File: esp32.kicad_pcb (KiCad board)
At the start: 2 copper layers, 44 x 100 mm, 129 parts, among them J1 USB_C, J10 UART_2, J11 I2C_0, J12 I2C_1, J13 I2C_2, J14 GND_CONN, J15 SPI_0, J16 SPI_1, J17 SPI_2, J18 PWR_CONN, J2 USB_C_UART, J3 A0, J4 A1, J5 A2, J6 D0, J7 D1, J8 UART_0, J9 UART_1, Q1 S8050, Q10 AO3400A, Q11 AO3400A, Q12 AO3400A, Q2 S8050, Q3 AO3400A, Q4 AO3400A, Q5 AO3400A, Q6 AO3400A, Q7 AO3400A, Q8 AO3400A, Q9 AO3400A, SW1 SW_RST, SW2 SW_BOOT, U1 AMS1117-3.3, U2 XL1509-5.0, U3 ESP32-S3-WROOM-1, U4 CH340C

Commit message: delete unused components
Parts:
- removed C11, C12, C13, C14, C15, C16: 100n, Capacitor_SMD:C_0805_2012Metric_Pad1.18x1.45mm_HandSolder
- removed D4: LED, LED_SMD:LED_0805_2012Metric_Pad1.15x1.40mm_HandSolder
- removed J10: UART_2, Connector_JST:JST_XH_B4B-XH-A_1x04_P2.50mm_Vertical
- removed J11: I2C_0, Connector_JST:JST_XH_B4B-XH-A_1x04_P2.50mm_Vertical
- removed J12: I2C_1, Connector_JST:JST_XH_B4B-XH-A_1x04_P2.50mm_Vertical
- removed J13: I2C_2, Connector_JST:JST_XH_B4B-XH-A_1x04_P2.50mm_Vertical
- removed J18: PWR_CONN, TerminalBlock:TerminalBlock_MaiXu_MX126-5.0-02P_1x02_P5.00mm
- removed J8: UART_0, Connector_JST:JST_XH_B4B-XH-A_1x04_P2.50mm_Vertical
- removed J9: UART_1, Connector_JST:JST_XH_B4B-XH-A_1x04_P2.50mm_Vertical
- removed R7: R, Resistor_SMD:R_0805_2012Metric_Pad1.20x1.40mm_HandSolder
- C17, C6, C8, D1, L1, U2: moved to F.Cu
- J14: value GND_CONN -> PWR_CONN
- moved C8 25.0 mm to (48.2, 35.0), turned to 0 degrees
- moved D5 22.4 mm to (62.0, 33.6), turned to 180 degrees
- moved U2 16.5 mm to (47.1, 42.4), turned to 0 degrees
- moved D1 14.0 mm to (62.4, 24.8), turned to 0 degrees
- moved L1 9.62 mm to (57.9, 40.4), turned to 0 degrees
- moved C17 8.98 mm to (64.8, 40.4), turned to 0 degrees
- moved C6 3.71 mm to (49.6, 25.9)
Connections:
- J14 pad 2: GND -> Net-(D5-A)
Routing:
- net Net-(D4-A): track 1.97 -> 0.00 mm

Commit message: LMR36520 version
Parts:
- removed C17: 47uF, Capacitor_THT:C_Radial_D6.3mm_H5.0mm_P2.50mm
- removed D1: SS34, Diode_SMD:D_SMB-SMC_Universal_Handsoldering
- removed U2: XL1509-5.0, Package_SO:SOIC-8_3.9x4.9mm_P1.27mm
- added C11: 22uF, Capacitor_SMD:C_0805_2012Metric_Pad1.18x1.45mm_HandSolder, F.Cu at (148.1, 83.9)
- added C12: 20pF, Capacitor_SMD:C_0805_2012Metric_Pad1.18x1.45mm_HandSolder, B.Cu at (148.8, 72.5)
- added R53: 43.2k, Resistor_SMD:R_0805_2012Metric_Pad1.20x1.40mm_HandSolder, B.Cu at (143.9, 70.4)
- added R7: 100k, Resistor_SMD:R_0805_2012Metric_Pad1.20x1.40mm_HandSolder, B.Cu at (148.8, 70.4)
- C4: value 10uF -> 4.7uF; moved to B.Cu
- C5: value 100nF -> 220nF; moved to B.Cu
- C6: value 470uF -> 1uF; footprint Capacitor_SMD:CP_Elec_8x10.5 -> Capacitor_SMD:C_0805_2012Metric_Pad1.18x1.45mm_HandSolder
- C7: value 10uF -> 0.1uF
- C8: value 180uF -> 22uF; footprint Capacitor_SMD:CP_Elec_6.3x5.4 -> Capacitor_SMD:C_0805_2012Metric_Pad1.18x1.45mm_HandSolder
- L1: value 68µH -> 10uH; footprint Inductor_SMD:L_6.3x6.3_H3 -> Inductor_SMD:L_Chilisin_BMRA00050530; moved to B.Cu
- U1: value AMS1117-3.3 -> LMR36520ADDAR; footprint Package_TO_SOT_SMD:SOT-223-3_TabPin2 -> Package_SO:Texas_HTSOP-8-1EP_3.9x4.9mm_P1.27mm_EP2.95x4.9mm_Mask2.4x3.1mm_ThermalVias
- moved C8 110.1 mm to (148.0, 81.8), turned to 180 degrees
- moved C6 108.6 mm to (147.0, 73.9), turned to -90 degrees
- moved L1 96.9 mm to (147.2, 78.1)
- moved D5 77.3 mm to (136.2, 55.3)
- moved C7 12.4 mm to (149.4, 73.9), turned to -90 degrees
- moved C4 5.82 mm to (147.0, 66.6), turned to -90 degrees
- moved C5 4.64 mm to (149.1, 66.6), turned to -90 degrees
- moved C20 3.05 mm to (152.2, 79.9)
- moved C18 3.05 mm to (152.3, 92.9)
- moved C19 3.05 mm to (152.3, 86.4)
- moved J15 2.70 mm to (166.4, 92.0)
- moved J16 2.70 mm to (166.4, 85.5)
- moved J17 2.70 mm to (166.4, 79.0)
- moved D3 2.12 mm to (149.3, 57.8)
- moved R6 2.12 mm to (145.3, 57.8)
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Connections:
- C4 pad 1: +3V3 -> VCC
- C5 pad 1: +3V3 -> VCC
- C6 pad 1: VCC -> Net-(U1-VCC)
- C7 pad 1: +5V -> Net-(U1-BOOT)
- C7 pad 2: GND -> Net-(U1-SW)
- C8 pad 1: +5V -> +3V3
- L1 pad 1: Net-(D1-K) -> Net-(U1-SW)
- L1 pad 2: +5V -> +3V3
- U1 pad 2: +3V3 -> VCC
- U1 pad 3: +5V -> VCC
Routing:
- net GND: track 697.3 -> 783.6 mm, vias 4 -> 5
- net +3V3: track 428.9 -> 454.9 mm, vias 26 -> 23
- net VCC: track 0.00 -> 21.6 mm, vias 0 -> 3
- net Net-(U1-SW): track 0.00 -> 10.7 mm, vias 0 -> 1
- net Net-(U1-FB): track 0.00 -> 5.02 mm, vias 0 -> 1
- net /flex_io3/OUT_0: track 4.99 -> 9.36 mm
- net /flex_io3/OUT_1: track 5.48 -> 9.63 mm
- net Net-(D5-A): track 0.00 -> 4.08 mm
- net /A0: track 143.9 -> 139.9 mm
- net Net-(U1-BOOT): track 0.00 -> 2.60 mm
- net Net-(U1-VCC): track 0.00 -> 2.52 mm
- net +5V: track 48.0 -> 45.5 mm, vias 6 -> 5
- net /SPI_CS0: track 55.4 -> 54.3 mm
- net /SPI_SCK: track 49.6 -> 48.5 mm
- net /SPI_MOSI: track 51.0 -> 49.9 mm
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
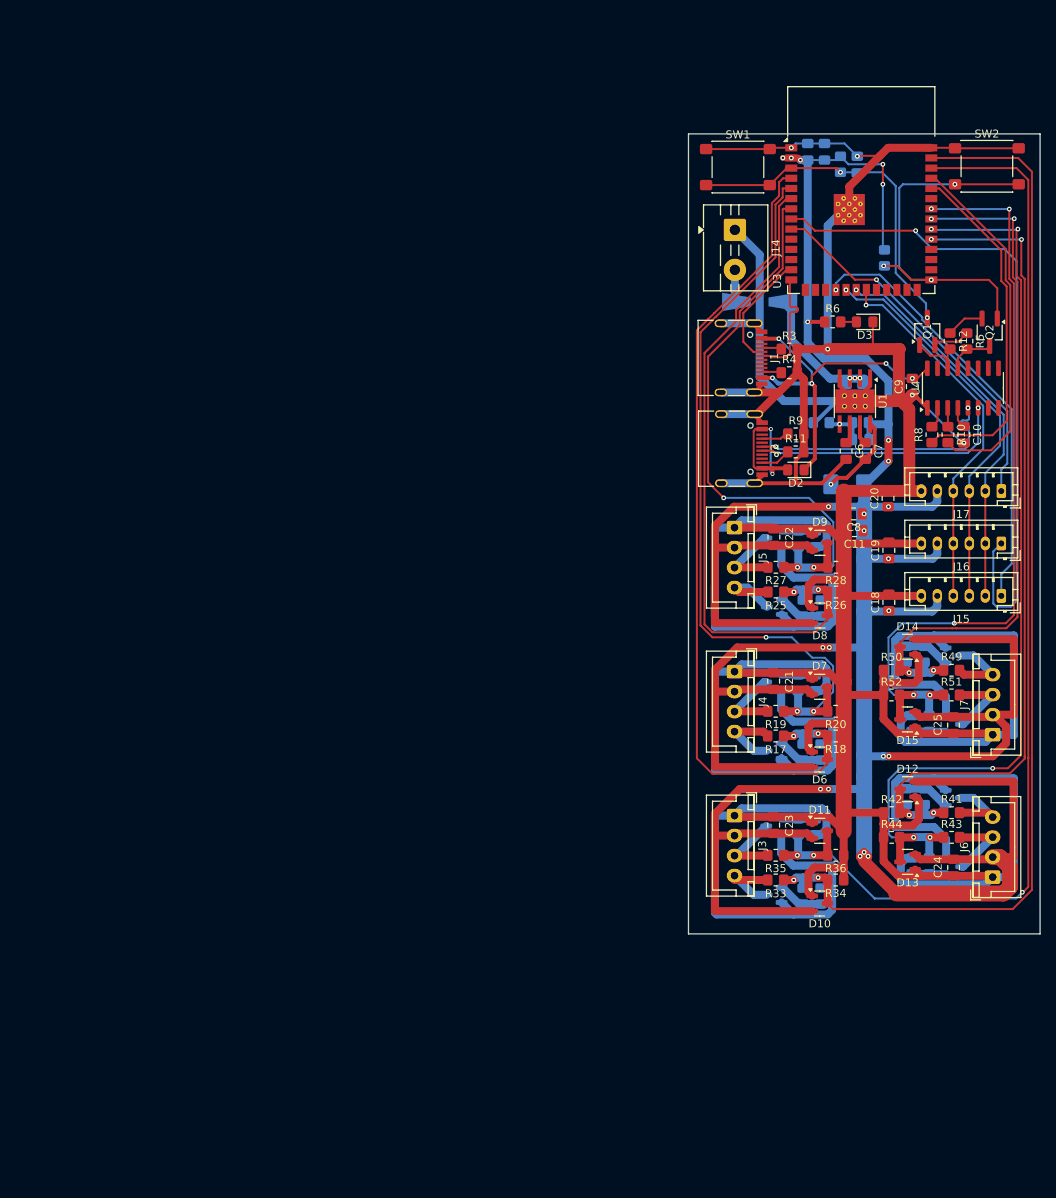
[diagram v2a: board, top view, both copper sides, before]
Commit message: rest components placed
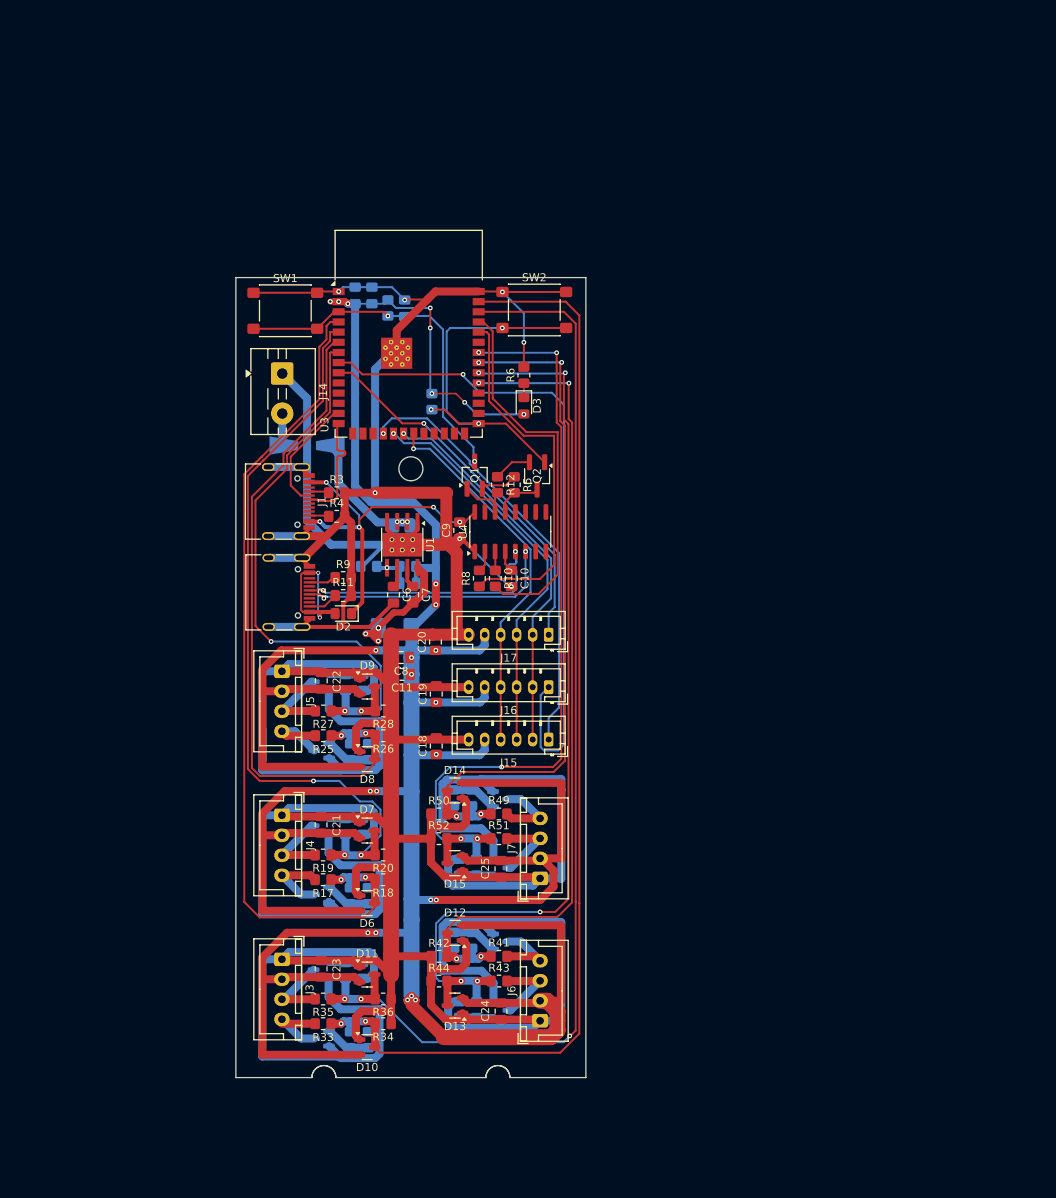
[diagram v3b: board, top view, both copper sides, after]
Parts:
- moved C1 59.4 mm to (87.7, 54.5)
- moved C12 59.4 mm to (92.3, 90.5)
- moved C22 59.4 mm to (81.4, 102.7)
- moved C3 59.4 mm to (91.8, 56.1)
- moved C7 59.4 mm to (92.8, 91.9)
- moved C8 59.4 mm to (91.4, 99.8)
- moved D8 59.4 mm to (87.2, 112.5)
- moved D9 59.4 mm to (87.2, 103.4)
- moved J1 59.4 mm to (75.8, 80.3)
- moved J15 59.4 mm to (109.8, 110.0)
- moved J16 59.4 mm to (109.8, 103.5)
- moved J17 59.4 mm to (109.8, 96.9)
- moved J2 59.4 mm to (75.9, 91.6)
- moved J7 59.4 mm to (108.8, 127.4)
- moved L1 59.4 mm to (90.6, 96.1)
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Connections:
- D3 pad 1: GND -> Net-(D3-K)
- D3 pad 2: Net-(D3-A) -> +3V3
- R6 pad 1: +3V3 -> Net-(D3-K)
- R6 pad 2: Net-(D3-A) -> GND
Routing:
- net +3V3: track 454.9 -> 465.3 mm, vias 23 -> 25
- net GND: track 783.6 -> 790.9 mm, vias 5 -> 7
- net Net-(U1-SW): track 10.7 -> 16.4 mm, vias 1 -> 7
- net /UART0_TX: track 45.2 -> 48.0 mm
- net /UART0_RX: track 44.0 -> 46.3 mm
- net /GPIO0: track 48.9 -> 46.6 mm
- net Net-(D3-A): track 1.98 -> 0.00 mm
- net Net-(D3-K): track 0.00 -> 1.80 mm
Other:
- board size 44 x 100 mm -> 43.8 x 100 mm

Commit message: with CH340
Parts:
- moved R3 0.80 mm to (83.5, 80.0)
- moved R4 0.12 mm to (83.5, 82.1)
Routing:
- net Net-(U1-SW): track 16.4 -> 20.0 mm, vias 7 -> 3
- net Net-(J1-CC1): track 2.52 -> 5.84 mm, vias 0 -> 2
- net /D+: track 14.6 -> 11.5 mm
- net /D-: track 14.6 -> 12.7 mm
- net Net-(U4-UD+): track 32.4 -> 30.9 mm
- net GND: track 790.9 -> 792.2 mm

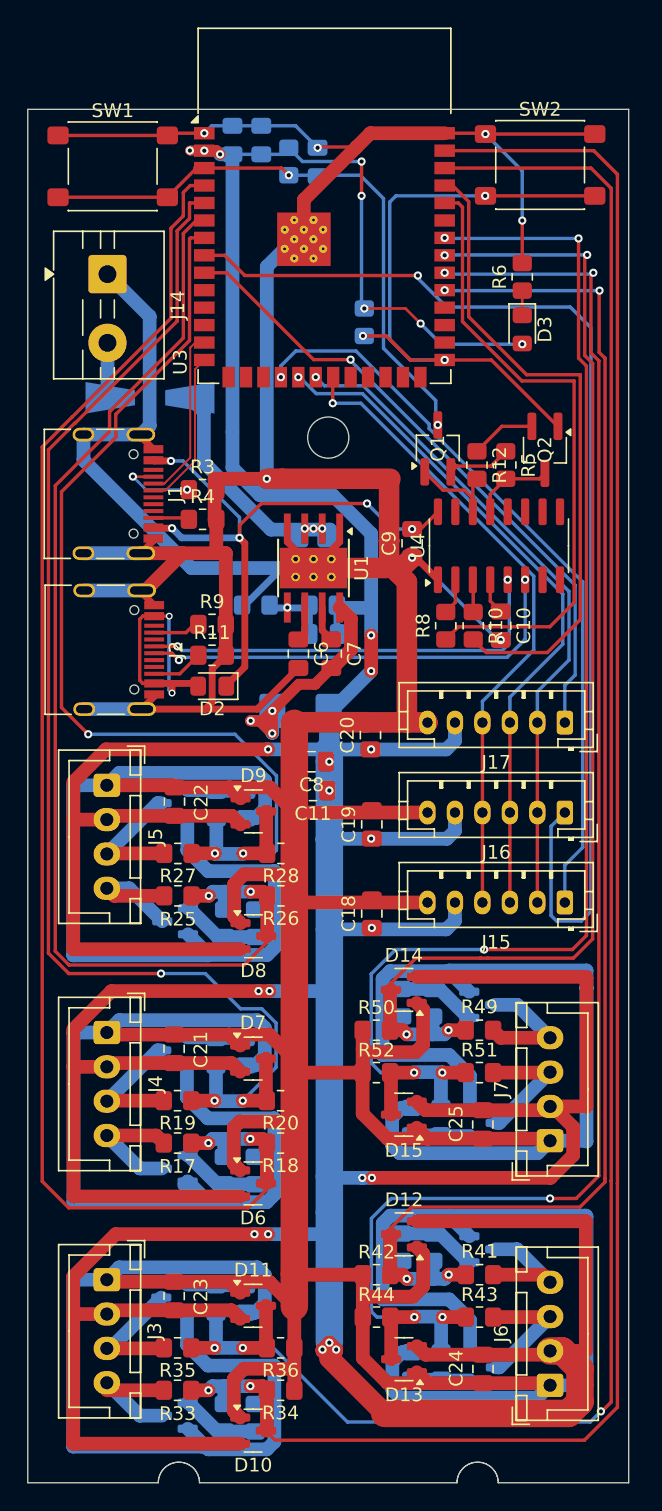
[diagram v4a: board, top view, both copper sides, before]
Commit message: without uart converter, small version
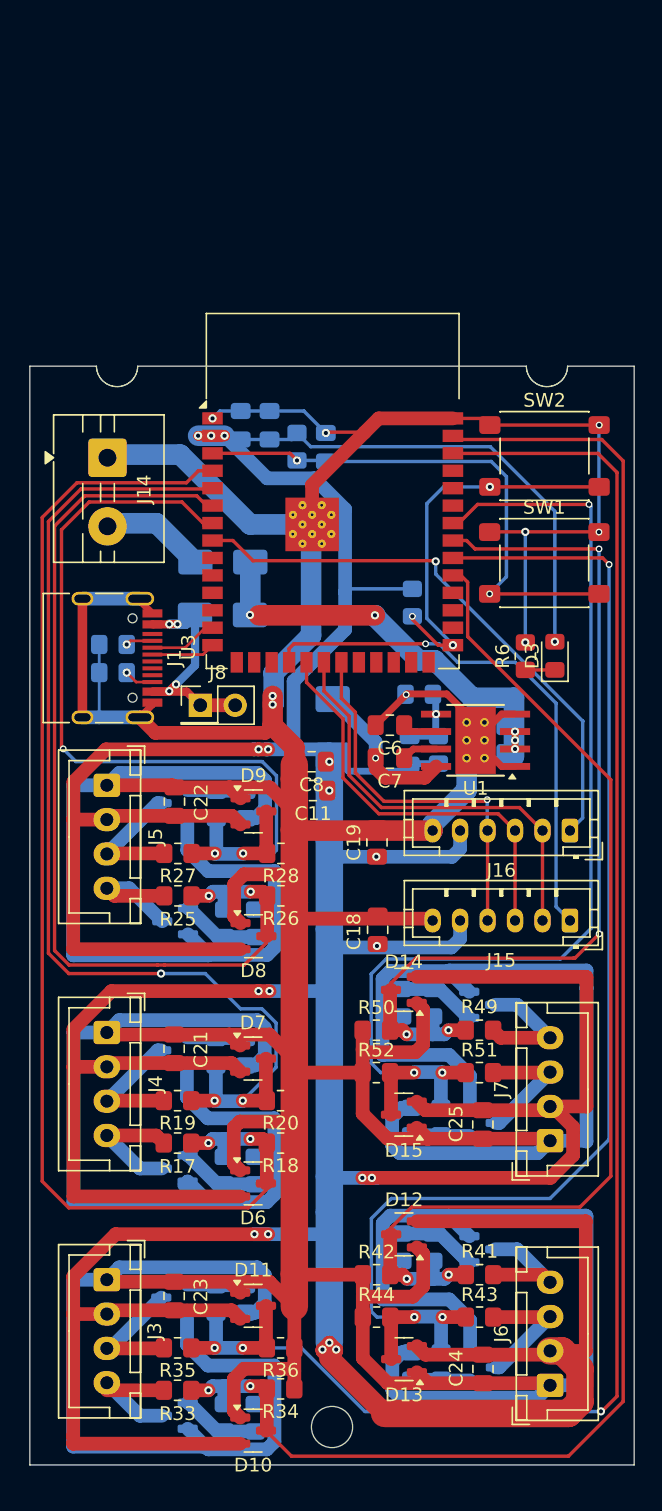
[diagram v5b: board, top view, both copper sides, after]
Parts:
- removed C10, C20, C9: 100n, Capacitor_SMD:C_0805_2012Metric_Pad1.18x1.45mm_HandSolder
- removed D2: D, Diode_SMD:D_0805_2012Metric_Pad1.15x1.40mm_HandSolder
- removed D5: SS34, Diode_SMD:D_SMA-SMB_Universal_Handsoldering
- removed J17: SPI_2, Connector_JST:JST_PH_B6B-PH-K_1x06_P2.00mm_Vertical
- removed J2: USB_C_UART, Connector_USB:USB_C_Receptacle_HRO_TYPE-C-31-M-12
- removed Q1, Q2: S8050, Package_TO_SOT_SMD:TSOT-23_HandSoldering
- removed R10, R8: 470R, Resistor_SMD:R_0805_2012Metric_Pad1.20x1.40mm_HandSolder
- removed R11, R9: 5.1K, Resistor_SMD:R_0805_2012Metric_Pad1.20x1.40mm_HandSolder
- removed R12, R5: 10k, Resistor_SMD:R_0805_2012Metric_Pad1.20x1.40mm_HandSolder
- removed U4: CH340C, Package_SO:SOIC-16_3.9x9.9mm_P1.27mm
- added D1: SS34, Diode_SMD:D_SMA, B.Cu at (84.9, 85.2)
- added D4: SS34, Diode_SMD:D_SMA, B.Cu at (84.9, 89.1)
- added J8: USB_VOUT, Connector_PinHeader_2.54mm:PinHeader_2x01_P2.54mm_Vertical, F.Cu at (83.3, 95.7)
- R3, R4: moved to B.Cu
- moved SW1 42.7 mm to (108.3, 85.3)
- moved R6 27.6 mm to (107.0, 92.1)
- moved D3 23.9 mm to (109.1, 92.0), turned to 90 degrees
- moved SW2 21.2 mm to (108.3, 77.5)
- moved C1 20.8 mm to (88.3, 75.3)
- moved C2 20.8 mm to (86.2, 75.3)
- moved R2 20.8 mm to (90.3, 76.8)
- moved U3 20.8 mm to (92.9, 80.0)
- moved C3 20.8 mm to (92.4, 76.9)
- moved R1 20.7 mm to (98.7, 88.2)
- moved C5 18.8 mm to (104.4, 99.2), turned to 180 degrees
- moved C4 18.7 mm to (104.4, 97.1), turned to 180 degrees
- moved U1 17.2 mm to (103.3, 98.2), turned to 180 degrees
- moved R53 13.6 mm to (99.2, 94.8)
- moved R7 13.5 mm to (100.6, 98.9), turned to -90 degrees
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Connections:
- net +5V renamed V_USB
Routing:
- net GND: track 792.2 -> 699.2 mm, vias 7 -> 9
- net /UART0_TX: track 48.0 -> 0.58 mm
- net /SPI_CS2: track 46.8 -> 0.00 mm, vias 1 -> 0
- net /UART0_RX: track 46.3 -> 0.00 mm
- net /SPI_CS1: track 84.3 -> 41.4 mm
- net Net-(U4-UD-): track 32.2 -> 0.00 mm, vias 2 -> 0
- net Net-(U4-UD+): track 30.9 -> 0.00 mm, vias 2 -> 0
- net /D0: track 103.8 -> 76.3 mm, vias 4 -> 2
- net V_USB: track 45.5 -> 20.3 mm, vias 5 -> 4
- net /D1: track 116.2 -> 94.5 mm, vias 5 -> 3
- net +3V3: track 465.3 -> 443.8 mm, vias 25 -> 19
- net /A1: track 142.1 -> 121.0 mm
- net /D2: track 87.0 -> 66.1 mm
- net /SPI_MOSI: track 49.9 -> 30.2 mm, vias 1 -> 0
- net /SPI_MISO: track 47.5 -> 27.8 mm
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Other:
- board size 43.8 x 100 mm -> 44 x 80 mm

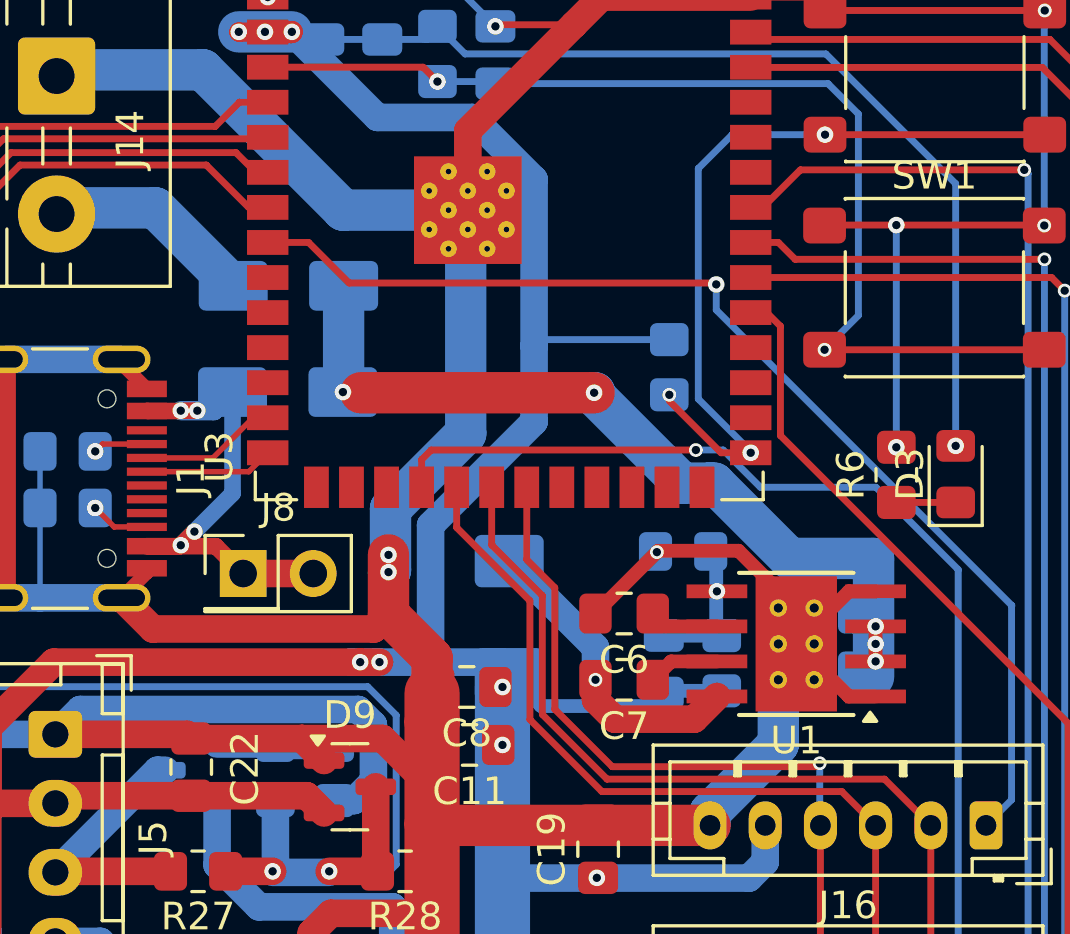
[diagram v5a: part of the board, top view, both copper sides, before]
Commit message: change footprints for better soldering
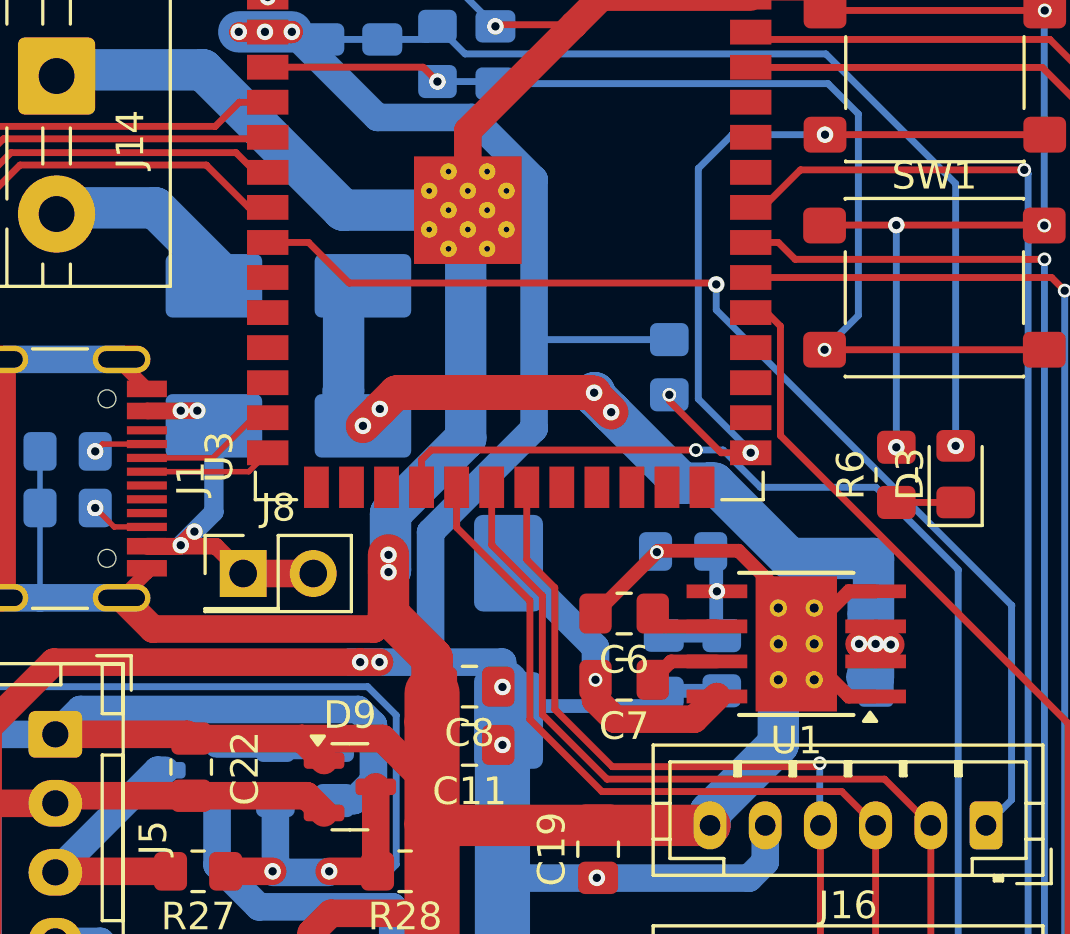
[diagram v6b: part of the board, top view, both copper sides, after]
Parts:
- removed D4: SS34, Diode_SMD:D_SMA
- added D2: SS34, Diode_SMD:D_SMB_Handsoldering, B.Cu at (84.9, 90.3)
- C4, C5: footprint Capacitor_SMD:C_0805_2012Metric_Pad1.18x1.45mm_HandSolder -> Library:C_1206&0805
- D1: footprint Diode_SMD:D_SMA -> Diode_SMD:D_SMB_Handsoldering
- moved L1 0.88 mm to (92.9, 98.1)
- moved C5 0.45 mm to (104.7, 99.5)
- moved C4 0.31 mm to (104.7, 97.0)
- moved C8 0.10 mm to (91.5, 99.8)
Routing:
- net VCC: track 34.5 -> 43.9 mm, vias 5 -> 7
- net V_USB: track 20.3 -> 17.9 mm
